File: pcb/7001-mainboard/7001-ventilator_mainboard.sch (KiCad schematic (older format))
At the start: 50 parts

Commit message: Cleanup first design
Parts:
- added J?: DNI, Connector_PinSocket_2.54mm:PinSocket_1x03_P2.54mm_Vertical, symbol Connector_Generic:Conn_01x03
- added R? (x2): 1k5, Resistor_SMD:R_0805_2012Metric, symbol Device:R
- C1, C10, C11, C12, C14, C16, C17, C19, C2, C3, C6, C7, C8, C9: renamed from C?; footprint Capacitor_SMD:C_0402_1005Metric -> Capacitor_SMD:C_0805_2012Metric
- C13, C15, C18, C4, C5: renamed from C?; footprint Capacitor_SMD:C_0603_1608Metric -> Capacitor_SMD:C_0805_2012Metric
- R1, R2, R3, R4, R5, R6, R7: renamed from R?; footprint Resistor_SMD:R_0402_1005Metric -> Resistor_SMD:R_0805_2012Metric
- gave numbers to parts that had none: 23
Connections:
- net labels added: +3.3V, I2C_SCL, I2C_SDA, ~ISP~, ~RESET~
- net labels removed: Vbus, button_~ISP~
- wire segments 117 -> 129
- no-connect marks 6 -> 4
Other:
- note added: "5V-based I2C\n\nNOTE: LPC11u is 5v-tolerant for I2C,\nflow sensors are 5V-based, but allow 2.5V as digital high"
- note added: "TODO flow sensor"
- note added: "TODO\n\n- 5v output header (display)\n- ADC in header\n- GPIO header\n- footprints voor sensors"
- note removed: "(open drain)"
- moved on the sheet: C7, TP1

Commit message: Add 0-20mA for pressure regulator
The pressure regulator can be adjusted via 4-20mA (SPI via AD5410)
The regulator has an on-board pressure sensor giving 4-20mA feedback, which
we convert to 0.6-3.0V for the ADC.
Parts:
- removed U4: MIC5501-3.0YM5, Package_TO_SOT_SMD:SOT-23-5, symbol Regulator_Linear:MIC5501-3.0YM5
- added C20, C24: 100nF 50V, Capacitor_SMD:C_0805_2012Metric, symbol Device:C
- added C21: 10uF 50V, Capacitor_SMD:C_1206_3216Metric, symbol Device:C
- added C22: 330uF, Jitter_Footprints:CP_Elec_12.5x13.5, symbol Device:CP
- added C23, C27: 10nF, Capacitor_SMD:C_0805_2012Metric, symbol Device:C
- added C25: 10uF, Capacitor_SMD:C_0805_2012Metric, symbol Device:C
- added C26: 100nF, Capacitor_SMD:C_0805_2012Metric, symbol Device:C
- added H2: DNI (mounting hole), MountingHole:MountingHole_3.5mm_Pad_Via, symbol Mechanical:MountingHole_Pad
- added J5, J7: TODO, symbol Connector_Generic:Conn_01x02
- added J6: 5V out, Connector_PinSocket_2.54mm:PinSocket_1x02_P2.54mm_Vertical, symbol Connector_Generic:Conn_01x02
- added J8: TODO, symbol Connector_Generic:Conn_01x03
- added R10, R12: 10k, Resistor_SMD:R_0805_2012Metric, symbol Device:R
- added R11, R13: 0, Resistor_SMD:R_0805_2012Metric, symbol Device:R
- added R14: DNI, Resistor_SMD:R_0805_2012Metric, symbol Device:R
- added R15: 150, Resistor_SMD:R_0805_2012Metric, symbol Device:R
- added U4: MCP1825S, symbol Regulator_Linear:MCP1825S
- added U7: AD5410AREZ, Jitter_Footprints:TSSOP-24-1EP_4.4x7.8mm_P0.65mm, symbol Jitter_Components:AD5410AREZ
- C13: value 1uF -> 4.7uF
- C14: value 100nF -> 10uF; Voltage rating 16V -> (none); purpose decoupling -> (none)
- C15: value 1uF -> 100nF; purpose decoupling -> (none)
- H1: footprint MountingHole:MountingHole_2.7mm_Pad_Via -> MountingHole:MountingHole_3.5mm_Pad_Via
- J2: value TODO -> SWD; footprint Jitter_Footprints:header_4x2.54_right_angle -> Connector_PinSocket_2.54mm:PinSocket_1x04_P2.54mm_Vertical
- TP1: value Reset -> 5V; footprint TestPoint:TestPoint_Pad_D1.0mm -> TestPoint:TestPoint_THTPad_D1.5mm_Drill0.7mm
- TP5: value 3V -> 5V; footprint TestPoint:TestPoint_Pad_D1.0mm -> TestPoint:TestPoint_THTPad_D1.5mm_Drill0.7mm
- gave numbers to parts that had none: 3
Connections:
- net labels added: +24V, A_PREG_PRESSURE, I_PREG_FEEDBACK, I_PREG_SETPOINT, MCU_DM, MCU_DP, PREG_CLEAR, PREG_OK, PREG_SPI_CLK, PREG_SPI_MISO, PREG_SPI_MOSI, PREG_SPI_~CS~
- wire segments 129 -> 189
- no-connect marks 4 -> 10
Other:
- note added: "24VDC 1.5A \nOUTPUT"
- note added: "24VDC 3A"
- note added: "3.3V LDO"
- note added: "4-20mA -> 0.6-3.0V\nLowpass filter:\n10k, 10nF = 1.6kHz"
- note added: "4-20mA input"
- note added: "4-20mA output"
- note added: "5V out\n(RPI display?)"
- note added: "ADC"
- note added: "Flow sensor"
- note added: "GPIO"
- note added: "Mogelijk handige copy-paste bouwblokjes"
- note added: "Power"
- note added: "Power Input"
- note added: "Pressure regulator (RP200_C_???)\n"
- note added: "Pressure sensor"
- note added: "SPI"
- note added: "TODO"
- note added: "TODO 24V 1.5A -> 5V3A"
- note added: "TODO\n\n- footprints voor sensors\n- extra on/off outputs (voltage? maybe relays?)\n- RPI hat board outline + Mouning holes\n- test points\n- I2C addr conflict check\n- ADC in header\n- GPIO header\n- 24V to 5V DC/DC? Or 5VDC from separate rpi PSU?"
- note removed: "3V LDO"
- note removed: "3V is used as the supply voltage for the microcontroller.\nThis LDO is always-on."
- note removed: "Mogelijk handige bouwblokjes"
- note removed: "TODO\n\n- 5v output header (display)\n- ADC in header\n- GPIO header\n- footprints voor sensors"
- moved on the sheet: C1, C10, C11, C12, C13, C16, C17, C18, C19, C2, C3, C4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

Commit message: Schematics: add RPI hat, refactor power section
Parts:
- removed F1: MCCFB1206TFF/2, Resistor_SMD:R_1206_3216Metric, symbol Device:Fuse_Small
- added C? (x2): 100nF, Capacitor_SMD:C_0805_2012Metric, symbol Device:C
- added J?: Raspberry_Pi_2_3, Connector_PinHeader_2.54mm:PinHeader_2x19_P2.54mm_Vertical_SMD, symbol Connector:Raspberry_Pi_2_3
- added J?: UART, Connector_PinSocket_2.54mm:PinSocket_1x04_P2.54mm_Vertical, symbol Connector_Generic:Conn_01x04
- added JP?: 5V_jumper, Connector_PinHeader_2.54mm:PinHeader_1x03_P2.54mm_Vertical, symbol Jumper:Jumper_3_Bridged12
- added R? (x2): 0, Resistor_SMD:R_0805_2012Metric, symbol Device:R
- J4: footprint Connector_PinSocket_2.54mm:PinSocket_1x03_P2.54mm_Vertical -> Connector_PinHeader_2.54mm:PinHeader_1x03_P2.54mm_Vertical
- J6: footprint Connector_PinSocket_2.54mm:PinSocket_1x02_P2.54mm_Vertical -> Connector_PinHeader_2.54mm:PinHeader_1x02_P2.54mm_Vertical
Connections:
- net labels added: DCDC_5V, RPI_RX, RPI_TX, USB_VBUS
- wire segments 189 -> 216
- no-connect marks 10 -> 38
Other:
- note added: "5V header for\nRPI display"
- note added: "Debug: SWD + UART"
- note added: "Jumper Option:\n1-2: power 5V from 24V DC/DC\n2-3: power 5V from USB\nNC: power 5V from Raspberry Pi"
- note added: "RPI hat"
- note added: "TODO pinswap these:"
- note added: "TODO\n\n- 24V to 5V DC/DC? Or 5VDC from separate rpi PSU?\n- footprints voor sensors\n- footprints voor screw terminals\n- extra on/off outputs (voltage? maybe relays?)\n- RPI hat connector + board outline + Mouning holes\n- test points\n- I2C addr conflict check\n- ADC in header\n- GPIO header"
- note removed: "5V out\n(RPI display?)"
- note removed: "Debugging: SWD\n(optional)"
- note removed: "Optional:\nUART header?"
- note removed: "TODO flow sensor"
- note removed: "TODO what current value?"
- note removed: "TODO\n\n- footprints voor sensors\n- extra on/off outputs (voltage? maybe relays?)\n- RPI hat board outline + Mouning holes\n- test points\n- I2C addr conflict check\n- ADC in header\n- GPIO header\n- 24V to 5V DC/DC? Or 5VDC from separate rpi PSU?"
- moved on the sheet: C1, C2, C3, C4, J6

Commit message: Schematics: add pressure sensors
The design allows 2 pressure sensors: 'sensor 1' and 'sensor 2'.

Only sensor 1 is required. Sensor 2 can be left out, but may be placed in case of
changing requirements in the future (e.g. using 2 sensors to measure
flow).

Each of the sensors may be implemented by choosing one of 3 different footprints.
On the PCB layout, these 3 footprints will be overlapped to create a
'universal' pressure sensor footprint.
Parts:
- removed C11, C16, C6: 100nF, Capacitor_SMD:C_0805_2012Metric, symbol Device:C
- removed C5: 1uF, Capacitor_SMD:C_0805_2012Metric, symbol Device:C
- removed C8: 47pF, Capacitor_SMD:C_0805_2012Metric, symbol Device:C
- removed C9: 2.2nF, Capacitor_SMD:C_0805_2012Metric, symbol Device:C
- removed R1: 68k, Resistor_SMD:R_0805_2012Metric, symbol Device:R
- removed R2: 100k, Resistor_SMD:R_0805_2012Metric, symbol Device:R
- removed TP2: sensor_out, TestPoint:TestPoint_Pad_D1.0mm, symbol Connector:TestPoint
- removed TP3: pressure_level, TestPoint:TestPoint_Pad_D1.0mm, symbol Connector:TestPoint
- removed TP4: LED_~CS~, TestPoint:TestPoint_Pad_D1.0mm, symbol Connector:TestPoint
- removed TP6: LED_CLK, TestPoint:TestPoint_Pad_D1.0mm, symbol Connector:TestPoint
- removed TP7: LED_clk_5V, TestPoint:TestPoint_Pad_D1.0mm, symbol Connector:TestPoint
- removed TP8: LED_MOSI, TestPoint:TestPoint_Pad_D1.0mm, symbol Connector:TestPoint
- removed TP9: LED_data_5V, TestPoint:TestPoint_Pad_D1.0mm, symbol Connector:TestPoint
- removed U1: TODO, symbol Sensor_Pressure:MPXH6115A
- removed U5, U6: 74AHCT1G125SE, Package_TO_SOT_SMD:SOT-353_SC-70-5, symbol 74xGxx:74AHCT1G125
- added R18: 0, Resistor_SMD:R_0805_2012Metric, symbol Device:R
- added R19: DNI, Resistor_SMD:R_0805_2012Metric, symbol Device:R
- J1: footprint Jitter_Footprints:USB_Micro-B_UJ2-MIBH-4-SMT-TR-67_SMD_Horizontal -> Connector_USB:USB_Micro-B_Molex_47346-0001
- J9: renamed from J?; footprint Connector_PinHeader_2.54mm:PinHeader_2x19_P2.54mm_Vertical_SMD -> Connector_PinHeader_2.54mm:PinHeader_2x20_P2.54mm_Vertical_SMD
- U4: footprint (none) -> Package_TO_SOT_SMD:SOT-223-3_TabPin2
- gave numbers to parts that had none: 6
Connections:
- net labels added: A_PRESSURE_1, A_PRESSURE_2, PSENSE_1_DATA_READY, PSENSE_1_SPI_~CS~, PSENSE_2_DATA_READY, PSENSE_2_SPI_~CS~, PSENSE_RESET, PSENSE_SPI_CLK, PSENSE_SPI_MISO, PSENSE_SPI_MOSI, V_PU
- net labels removed: LED_CLK, LED_MOSI, LED_clock_5V, LED_data_5V, LED_~CS~, pressure_level, pressure_sensor_out
- wire segments 216 -> 205
- no-connect marks 38 -> 36
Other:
- note added: "NOTE: LPC11u is 5v-tolerant for I2C,\nflow sensors are 5V-based, but allow 2.5V as digital high,\npressure sensor is 3.3V-based, unknown if 5V-tolerant"
- note added: "Pressure sensor(s)"
- note removed: "3V to 5V level shifting"
- note removed: "5V to 3V divider.\nRC filter: 40kOhm, 2.2nF: Fc= 1.8Khz\n"
- note removed: "5V-based I2C\n\nNOTE: LPC11u is 5v-tolerant for I2C,\nflow sensors are 5V-based, but allow 2.5V as digital high"
- note removed: "Place close to\nADC input"
- note removed: "Pressure sensor"
- moved on the sheet: C10, C12, C17, C18, C19, C2, C22, C3, C4, C7, D1, H1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

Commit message: Schematics/PCB: add screw terminal footprints
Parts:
- J5: value TODO -> 24VIN; footprint (none) -> Jitter_Footprints:TerminalBlock_Wurth_WR-TBL_691322110002_1x02_P3.50mm_Horizontal
- J7: value TODO -> PREG_PWR; footprint (none) -> Jitter_Footprints:TerminalBlock_Wurth_WR-TBL_691322110002_1x02_P3.50mm_Horizontal
- J8: value TODO -> PREG_SIGNALS; footprint (none) -> Jitter_Footprints:TerminalBlock_Wurth_WR-TBL_691322110003_1x03_P3.50mm_Horizontal
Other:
- note added: "TODO\n\n- 24V to 5V DC/DC? Or 5VDC from separate rpi PSU?\n- RPI hat connector + board outline + Mouning holes\n- extra on/off outputs (voltage? maybe relays?)\n- test points\n- I2C addr conflict check\n- ADC in header\n- GPIO header"
- note removed: "TODO\n\n- 24V to 5V DC/DC? Or 5VDC from separate rpi PSU?\n- footprints voor sensors\n- footprints voor screw terminals\n- extra on/off outputs (voltage? maybe relays?)\n- RPI hat connector + board outline + Mouning holes\n- test points\n- I2C addr conflict check\n- ADC in header\n- GPIO header"
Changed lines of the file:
@@
 	3700 4950 3700 5600
 Text Notes 700  10750 0    118  ~ 0
-TODO\n\n- 24V to 5V DC/DC? Or 5VDC from separate rpi PSU?\n- footprints voor sensors\n- footprints voor screw terminals\n- extra on/off outputs (voltage? maybe relays?)\n- RPI hat connector + board outline + Mouning holes\n- test points\n- I2C addr conflict check\n- ADC in header\n- GPIO header
+TODO\n\n- 24V to 5V DC/DC? Or 5VDC from separate rpi PSU?\n- RPI hat connector + board outline + Mouning holes\n- extra on/off outputs (voltage? maybe relays?)\n- test points\n- I2C addr conflict check\n- ADC in header\n- GPIO header
 Wire Wire Line
 	1050 7800 1000 7800
@@
 AR Path="/5BF2E340/5EAD36B5" Ref="J?"  Part="1"
 AR Path="/5EAD36B5" Ref="J8"  Part="1"
-F 0 "J8" H 15700 2800 50  0000 C CNN
-F 1 "TODO" H 15700 2900 50  0000 C CNN
-F 2 "" H 15700 3100 50  0001 C CNN
+F 0 "J8" H 15700 2900 50  0000 C CNN
+F 1 "PREG_SIGNALS" H 15700 2900 50  0001 C CNN
+F 2 "Jitter_Footprints:TerminalBlock_Wurth_WR-TBL_691322110003_1x03_P3.50mm_Horizontal" H 15700 3100 50  0001 C CNN
 F 3 "~" H 15700 3100 50  0001 C CNN
 	1    15700 3100
@@
 AR Path="/5BF2E340/5EB10B69" Ref="J?"  Part="1"
 AR Path="/5EB10B69" Ref="J7"  Part="1"
-F 0 "J7" H 15700 2050 50  0000 C CNN
-F 1 "TODO" H 15700 2150 50  0000 C CNN
-F 2 "" H 15700 2350 50  0001 C CNN
+F 0 "J7" H 15700 2150 50  0000 C CNN
+F 1 "PREG_PWR" H 15700 2150 50  0001 C CNN
+F 2 "Jitter_Footprints:TerminalBlock_Wurth_WR-TBL_691322110002_1x02_P3.50mm_Horizontal" H 15700 2350 50  0001 C CNN
 F 3 "~" H 15700 2350 50  0001 C CNN
 	1    15700 2350
@@
 AR Path="/5EBE6F1F" Ref="J5"  Part="1"
 F 0 "J5" H 1050 1550 50  0000 C CNN
-F 1 "TODO" H 1050 1650 50  0000 C CNN
-F 2 "" H 1050 1850 50  0001 C CNN
+F 1 "24VIN" H 1050 1650 50  0000 C CNN
+F 2 "Jitter_Footprints:TerminalBlock_Wurth_WR-TBL_691322110002_1x02_P3.50mm_Horizontal" H 1050 1850 50  0001 C CNN
 F 3 "~" H 1050 1850 50  0001 C CNN
 	1    1050 1850

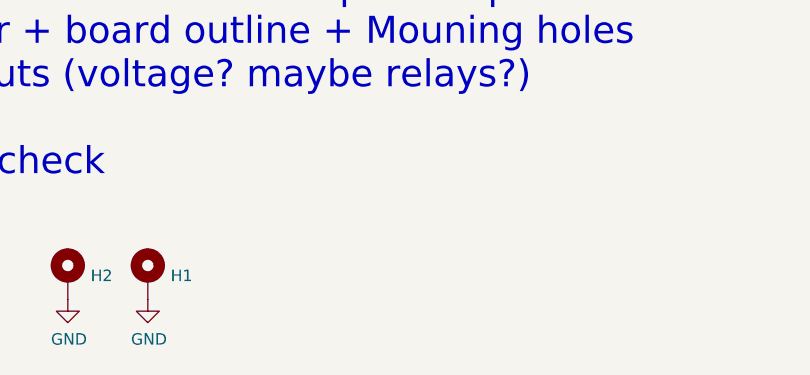
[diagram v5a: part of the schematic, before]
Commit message: Schematics/PCB: mounting holes, group components in layout
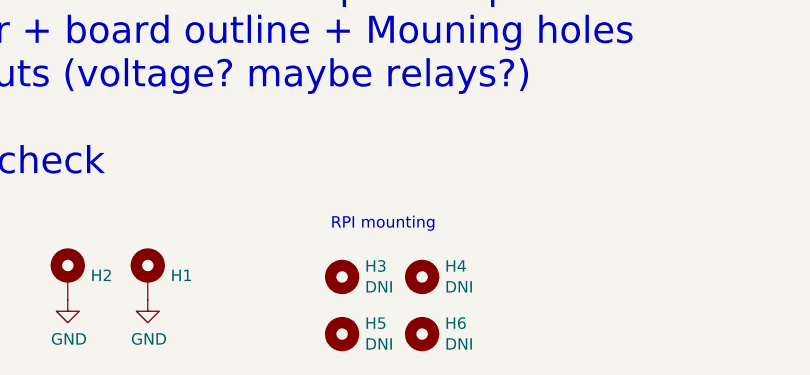
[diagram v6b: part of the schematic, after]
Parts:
- added H3, H4, H5, H6: DNI, MountingHole:MountingHole_2.7mm_M2.5, symbol Mechanical:MountingHole
- J9: footprint Connector_PinHeader_2.54mm:PinHeader_2x20_P2.54mm_Vertical_SMD -> Connector_PinSocket_2.54mm:PinSocket_2x20_P2.54mm_Vertical_SMD
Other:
- note added: "RPI mounting"
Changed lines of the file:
@@
 Comment4 ""
 $EndDescr
-$Comp
-L Mechanical:MountingHole_Pad H1
-U 1 1 5C0E7FF6
-P 2850 10800
-F 0 "H1" H 2950 10805 50  0000 L CNN
-F 1 "DNI (mounting hole)" H 2950 10760 50  0001 L CNN
-F 2 "MountingHole:MountingHole_3.5mm_Pad_Via" H 2850 10800 50  0001 C CNN
-F 3 "~" H 2850 10800 50  0001 C CNN
-	1    2850 10800
-	1    0    0    -1
-$EndComp
-$Comp
-L power:GND #PWR0119
-U 1 1 5C0E807D
-P 2850 10900
-F 0 "#PWR0119" H 2850 10650 50  0001 C CNN
-F 1 "GND" H 2855 10727 50  0000 C CNN
-F 2 "" H 2850 10900 50  0001 C CNN
-F 3 "" H 2850 10900 50  0001 C CNN
-	1    2850 10900
-	1    0    0    -1
-$EndComp
 Text Label 2350 5300 2    50   ~ 0
 USB_DP
@@
 Wire Wire Line
 	3700 4950 3700 5600
-Text Notes 700  10750 0    118  ~ 0
-TODO\n\n- 24V to 5V DC/DC? Or 5VDC from separate rpi PSU?\n- RPI hat connector + board outline + Mouning holes\n- extra on/off outputs (voltage? maybe relays?)\n- test points\n- I2C addr conflict check\n- ADC in header\n- GPIO header
 Wire Wire Line
 	1050 7800 1000 7800
@@
 Wire Wire Line
 	12400 4400 12800 4400
-$Comp
-L Mechanical:MountingHole_Pad H2
-U 1 1 5EAC584F
-P 2500 10800
-F 0 "H2" H 2600 10805 50  0000 L CNN
-F 1 "DNI (mounting hole)" H 2600 10760 50  0001 L CNN
-F 2 "MountingHole:MountingHole_3.5mm_Pad_Via" H 2500 10800 50  0001 C CNN
-F 3 "~" H 2500 10800 50  0001 C CNN
-	1    2500 10800
-	1    0    0    -1
-$EndComp
-$Comp
-L power:GND #PWR022
-U 1 1 5EAC5855
-P 2500 10900
-F 0 "#PWR022" H 2500 10650 50  0001 C CNN
-F 1 "GND" H 2505 10727 50  0000 C CNN
-F 2 "" H 2500 10900 50  0001 C CNN
-F 3 "" H 2500 10900 50  0001 C CNN
-	1    2500 10900
-	1    0    0    -1
-$EndComp
 $Comp
 L Connector_Generic:Conn_01x03 J?
@@
 F 0 "J9" H 8750 1150 50  0000 C CNN
 F 1 "Raspberry_Pi_2_3" H 9050 1050 50  0000 C CNN
-F 2 "Connector_PinHeader_2.54mm:PinHeader_2x20_P2.54mm_Vertical_SMD" H 8900 2550 50  0001 C CNN
+F 2 "Connector_PinSocket_2.54mm:PinSocket_2x20_P2.54mm_Vertical_SMD" H 8900 2550 50  0001 C CNN
 F 3 "https://www.raspberrypi.org/documentation/hardware/raspberrypi/schematics/rpi_SCH_3bplus_1p0_reduced.pdf" H 8900 2550 50  0001 C CNN
 	1    8900 2550
@@
 Wire Wire Line
 	1050 7750 1050 7800
+$Comp
+L Mechanical:MountingHole H3
+U 1 1 5F955C5F
+P 3700 10800
+F 0 "H3" H 3800 10846 50  0000 L CNN
+F 1 "DNI" H 3800 10755 50  0000 L CNN
+F 2 "MountingHole:MountingHole_2.7mm_M2.5" H 3700 10800 50  0001 C CNN
+F 3 "~" H 3700 10800 50  0001 C CNN
+	1    3700 10800
+	1    0    0    -1
+$EndComp
+$Comp
+L Mechanical:MountingHole H4
+U 1 1 5F95D0C5
+P 4050 10800
+F 0 "H4" H 4150 10846 50  0000 L CNN
+F 1 "DNI" H 4150 10755 50  0000 L CNN
+F 2 "MountingHole:MountingHole_2.7mm_M2.5" H 4050 10800 50  0001 C CNN
+F 3 "~" H 4050 10800 50  0001 C CNN
+	1    4050 10800
+	1    0    0    -1
+$EndComp
+$Comp
+L Mechanical:MountingHole H6
+U 1 1 5F95D34E
+P 4050 11050
+F 0 "H6" H 4150 11096 50  0000 L CNN
+F 1 "DNI" H 4150 11005 50  0000 L CNN
+F 2 "MountingHole:MountingHole_2.7mm_M2.5" H 4050 11050 50  0001 C CNN
+F 3 "~" H 4050 11050 50  0001 C CNN
+	1    4050 11050
+	1    0    0    -1
+$EndComp
+$Comp
+L Mechanical:MountingHole H5
+U 1 1 5F95D61B
+P 3700 11050
+F 0 "H5" H 3800 11096 50  0000 L CNN
+F 1 "DNI" H 3800 11005 50  0000 L CNN
+F 2 "MountingHole:MountingHole_2.7mm_M2.5" H 3700 11050 50  0001 C CNN
+F 3 "~" H 3700 11050 50  0001 C CNN
+	1    3700 11050
+	1    0    0    -1
+$EndComp
+Text Notes 3650 10600 0    50   ~ 0
+RPI mounting
+$Comp
+L power:GND #PWR022
+U 1 1 5EAC5855
+P 2500 10900
+F 0 "#PWR022" H 2500 10650 50  0001 C CNN
+F 1 "GND" H 2505 10727 50  0000 C CNN
+F 2 "" H 2500 10900 50  0001 C CNN
+F 3 "" H 2500 10900 50  0001 C CNN
+	1    2500 10900
+	1    0    0    -1
+$EndComp
+$Comp
+L Mechanical:MountingHole_Pad H2
+U 1 1 5EAC584F
+P 2500 10800
+F 0 "H2" H 2600 10805 50  0000 L CNN
+F 1 "DNI (mounting hole)" H 2600 10760 50  0001 L CNN
+F 2 "MountingHole:MountingHole_3.5mm_Pad_Via" H 2500 10800 50  0001 C CNN
+F 3 "~" H 2500 10800 50  0001 C CNN
+	1    2500 10800
+	1    0    0    -1
+$EndComp
+Text Notes 700  10750 0    118  ~ 0
+TODO\n\n- 24V to 5V DC/DC? Or 5VDC from separate rpi PSU?\n- RPI hat connector + board outline + Mouning holes\n- extra on/off outputs (voltage? maybe relays?)\n- test points\n- I2C addr conflict check\n- ADC in header\n- GPIO header
+$Comp
+L power:GND #PWR0119
+U 1 1 5C0E807D
+P 2850 10900
+F 0 "#PWR0119" H 2850 10650 50  0001 C CNN
+F 1 "GND" H 2855 10727 50  0000 C CNN
+F 2 "" H 2850 10900 50  0001 C CNN
+F 3 "" H 2850 10900 50  0001 C CNN
+	1    2850 10900
+	1    0    0    -1
+$EndComp
+$Comp
+L Mechanical:MountingHole_Pad H1
+U 1 1 5C0E7FF6
+P 2850 10800
+F 0 "H1" H 2950 10805 50  0000 L CNN
+F 1 "DNI (mounting hole)" H 2950 10760 50  0001 L CNN
+F 2 "MountingHole:MountingHole_3.5mm_Pad_Via" H 2850 10800 50  0001 C CNN
+F 3 "~" H 2850 10800 50  0001 C CNN
+	1    2850 10800
+	1    0    0    -1
+$EndComp
 $EndSCHEMATC

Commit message: Schematics: add 24v,12v power supplies, etc
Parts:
- added C? (x2): 100nF, Capacitor_SMD:C_0805_2012Metric, symbol Device:C
- added C? (x2): 10uF 50V, Capacitor_SMD:C_1206_3216Metric, symbol Device:C
- added C? (x3): 100nF 50V, Capacitor_SMD:C_0805_2012Metric, symbol Device:C
- added C?: 10uF, Capacitor_SMD:C_0805_2012Metric, symbol Device:C
- added C?: 1uF, Capacitor_SMD:C_0805_2012Metric, symbol Device:C
- added J?: I2C, Jitter_Footprints:TerminalBlock_Wurth_WR-TBL_691322110004_1x04_P3.50mm_Horizontal, symbol Connector_Generic:Conn_01x04
- added J?: FLOW_SENSORS, Jitter_Footprints:TerminalBlock_Wurth_WR-TBL_691322110003_1x03_P3.50mm_Horizontal, symbol Connector_Generic:Conn_01x03
- added J?: 12V, Jitter_Footprints:TerminalBlock_Wurth_WR-TBL_691322110002_1x02_P3.50mm_Horizontal, symbol Connector_Generic:Conn_01x02
- added R?: 1k5, Resistor_SMD:R_0805_2012Metric, symbol Device:R
- added R?: 68k, Resistor_SMD:R_0805_2012Metric, symbol Device:R
- added R? (x2): DNI, Resistor_SMD:R_0805_2012Metric, symbol Device:R
- added R?: 3.3k, Resistor_SMD:R_0805_2012Metric, symbol Device:R
- added R?: 10k, Resistor_SMD:R_0805_2012Metric, symbol Device:R
- added U?: LM2937IMP-12/NOPB, Package_TO_SOT_SMD:SOT-223-3_TabPin2, symbol Regulator_Linear:MCP1825S
- added U?: S24SE05004PDFA_DC-DC, symbol Jitter_Components:S24SE05004PDFA_DC-DC
- U4: value MCP1825S -> MCP1825S-3302E; Farnell (none) -> 1578404; MPN (none) -> MCP1825S-3302E
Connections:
- net labels added: +12V, A_FLOW, UART_DBG_RX, UART_DBG_TX
- wire segments 205 -> 238
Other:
- note added: "12VDC 25mA"
- note added: "24V -> 12V LDO (40mA)"
- note added: "24V 1.5A -> 5V3A"
- note added: "Flow sensor (10V analog)"
- note added: "I2C port"
- note added: "Scale 12V input to ca 3V\nLowpass fc ca 600Hz"
- note added: "TODO DIFFERENT UART?"
- note added: "TODO\n\n- extra on/off outputs (voltage? maybe relays?)\n- test points\n- ADC in header\n- GPIO header"
- note added: "extra UART"
- note added: "floating input\nshould also\nenable power"
- note added: "optional output\nvoltage trim"
- note removed: "Flow sensor"
- note removed: "TODO"
- note removed: "TODO 24V 1.5A -> 5V3A"
- note removed: "TODO\n\n- 24V to 5V DC/DC? Or 5VDC from separate rpi PSU?\n- RPI hat connector + board outline + Mouning holes\n- extra on/off outputs (voltage? maybe relays?)\n- test points\n- I2C addr conflict check\n- ADC in header\n- GPIO header"
- moved on the sheet: C1, C10, C12, C13, C2, C25, C3, C4, C7, J1, J10, J2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
